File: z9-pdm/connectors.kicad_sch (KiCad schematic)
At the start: 11 parts, among them J10 RedCubeTerminal, J11 RedCubeTerminal, J12 Wago 12 pin 1 level 3.5mm 260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, J16 JST GH, J17 Wago 12 pin 1 level 3.5mm 260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, J19 Wago 12 pin 1 level 3.5mm 260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, J200 TE_DT15-12PC-B016 -Conn_01x12, J201 TE_DT15-12PC-B016 -Conn_01x12, J202 TE_DT15-12PC-B016 -Conn_01x12, J203 TE_DT15-12PC-B016 -Conn_01x12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

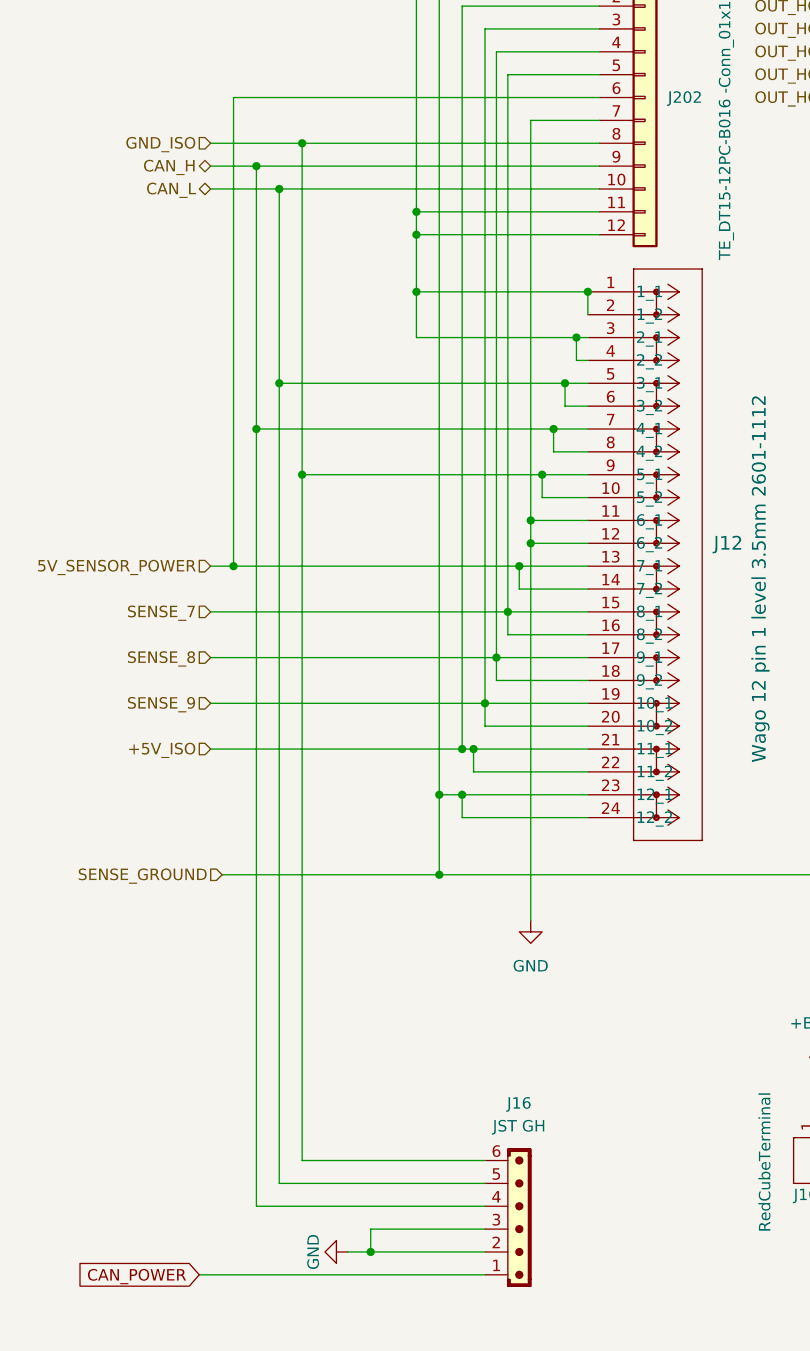
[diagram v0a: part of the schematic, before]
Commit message: laypout ad section canl/h swap
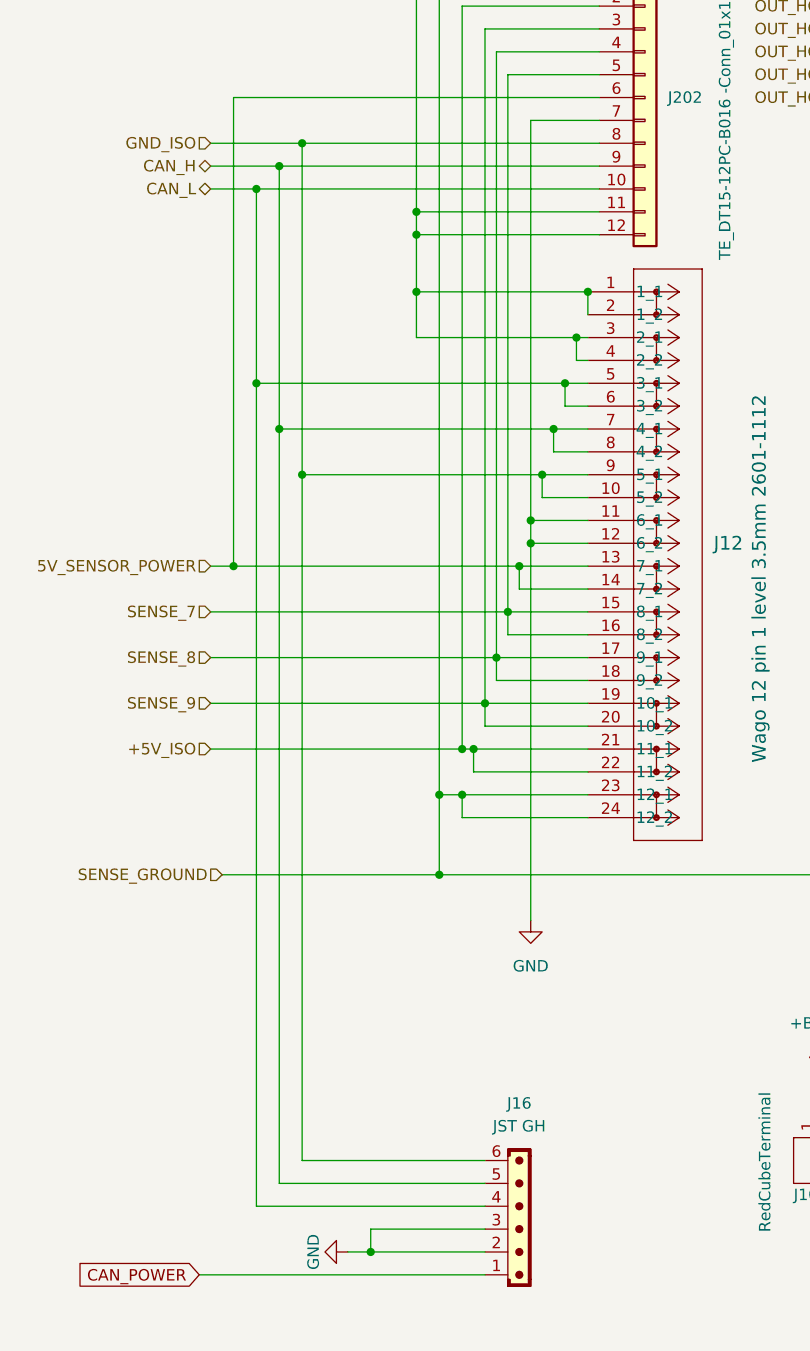
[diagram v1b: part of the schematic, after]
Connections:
- net CAN_H: now also J16.5; no longer J16.4
- net CAN_L: now also J16.4; no longer J16.5

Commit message: routing
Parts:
- J11: Voltage (none) -> GROUND
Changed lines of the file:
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@@
 			)
 		)
-		(property "Voltage" ""
+		(property "Voltage" "GROUND"
 			(at 107.95 162.56 90)
 			(effects

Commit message: new fuse and ideal diode
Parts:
- J10, J11, J12, J17, J19, J200, J201, J202, J203, J21: now not fitted; now left out of the parts list
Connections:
- net +12V_VIPOWER is gone; now on net +BATT: J12.1 (1_1), J12.2 (1_2), J12.3 (2_1), J12.4 (2_2), J202.11 (Pin_11), J202.12 (Pin_12)
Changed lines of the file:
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@@
 		(unit 1)
 		(exclude_from_sim no)
-		(in_bom yes)
+		(in_bom no)
 		(on_board yes)
-		(dnp no)
+		(dnp yes)
 		(property "Reference" "J17"
 			(at 270.51 92.7099 0)
@@
 		(unit 1)
 		(exclude_from_sim no)
-		(in_bom yes)
-		(on_board yes)
-		(dnp no)
+		(in_bom no)
+		(on_board no)
+		(dnp yes)
 		(property "Reference" "J11"
 			(at 110.49 157.48 90)
@@
 		(unit 1)
 		(exclude_from_sim no)
-		(in_bom yes)
+		(in_bom no)
 		(on_board yes)
-		(dnp no)
+		(dnp yes)
 		(property "Reference" "J202"
 			(at 83.82 43.1799 0)
@@
 			)
 		)
-		(property "Value" "+12V_VIPOWER"
+		(property "Value" "+BATT"
 			(at 25.4 21.59 0)
 			(effects
@@
 		(unit 1)
 		(exclude_from_sim no)
-		(in_bom yes)
+		(in_bom no)
 		(on_board yes)
-		(dnp no)
+		(dnp yes)
 		(property "Reference" "J21"
 			(at 143.51 92.7099 0)
@@
 		(unit 1)
 		(exclude_from_sim no)
-		(in_bom yes)
+		(in_bom no)
 		(on_board yes)
-		(dnp no)
+		(dnp yes)
 		(property "Reference" "J200"
 			(at 138.43 43.1799 0)
@@
 		(unit 1)
 		(exclude_from_sim no)
-		(in_bom yes)
+		(in_bom no)
 		(on_board yes)
-		(dnp no)
+		(dnp yes)
 		(property "Reference" "J201"
 			(at 198.12 43.1799 0)
@@
 		(unit 1)
 		(exclude_from_sim no)
-		(in_bom yes)
+		(in_bom no)
 		(on_board yes)
-		(dnp no)
+		(dnp yes)
 		(property "Reference" "J203"
 			(at 265.43 43.1799 0)
@@
 		(unit 1)
 		(exclude_from_sim no)
-		(in_bom yes)
+		(in_bom no)
 		(on_board yes)
-		(dnp no)
+		(dnp yes)
 		(property "Reference" "J10"
 			(at 97.79 165.1 90)
@@
 		(unit 1)
 		(exclude_from_sim no)
-		(in_bom yes)
+		(in_bom no)
 		(on_board yes)
-		(dnp no)
+		(dnp yes)
 		(property "Reference" "J19"
 			(at 220.98 92.7099 0)
@@
 		(unit 1)
 		(exclude_from_sim no)
-		(in_bom yes)
+		(in_bom no)
 		(on_board yes)
-		(dnp no)
+		(dnp yes)
 		(property "Reference" "J12"
 			(at 88.9 92.7099 0)

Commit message: post 5v lay references lost
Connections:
- net +5V_ISO is gone; now on net GND: J12.21 (11_1), J12.22 (11_2), J202.2 (Pin_2)
- net CAN_POWER: now also J12.10 (5_2), J12.9 (5_1), J202.7 (Pin_7)
- net GND: no longer J12.11 (6_1), J12.12 (6_2), J202.7 (Pin_7)
- net GND_ISO: now also J12.11 (6_1), J12.12 (6_2); no longer J12.10 (5_2), J12.9 (5_1)
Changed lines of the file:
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@@
 	)
 	(junction
-		(at 68.58 90.17)
-		(diameter 0)
-		(color 0 0 0 0)
-	)
-	(junction
 		(at 55.88 105.41)
 		(diameter 0)
@@
 	)
 	(junction
-		(at 40.64 30.48)
+		(at 72.39 45.72)
 		(diameter 0)
 		(color 0 0 0 0)
 	)
 	(junction
-		(at 43.18 85.09)
+		(at 40.64 30.48)
 		(diameter 0)
 		(color 0 0 0 0)
@@
 	)
 	(junction
+		(at 74.93 85.09)
+		(diameter 0)
+		(color 0 0 0 0)
+	)
+	(junction
 		(at 165.1 50.8)
 		(diameter 0)
@@
 	)
 	(junction
-		(at 256.54 74.93)
+		(at 68.58 48.26)
 		(diameter 0)
 		(color 0 0 0 0)
 	)
 	(junction
-		(at 129.54 64.77)
+		(at 256.54 74.93)
 		(diameter 0)
 		(color 0 0 0 0)
 	)
 	(junction
-		(at 129.54 105.41)
+		(at 129.54 64.77)
 		(diameter 0)
 		(color 0 0 0 0)
 	)
 	(junction
-		(at 232.41 100.33)
+		(at 129.54 105.41)
 		(diameter 0)
 		(color 0 0 0 0)
 	)
 	(junction
-		(at 74.93 85.09)
+		(at 232.41 100.33)
 		(diameter 0)
 		(color 0 0 0 0)
@@
 	(wire
 		(pts
+			(xy 72.39 45.72) (xy 76.2 45.72)
+		)
+		(stroke
+			(width 0)
+			(type default)
+		)
+	)
+	(wire
+		(pts
 			(xy 165.1 110.49) (xy 189.23 110.49)
 		)
@@
 	(wire
 		(pts
-			(xy 43.18 48.26) (xy 43.18 85.09)
+			(xy 43.18 48.26) (xy 43.18 161.29)
 		)
 		(stroke
@@
 	(wire
 		(pts
-			(xy 68.58 45.72) (xy 68.58 90.17)
-		)
-		(stroke
-			(width 0)
-			(type default)
-		)
-	)
-	(wire
-		(pts
 			(xy 48.26 120.65) (xy 74.93 120.65)
 		)
@@
 	(wire
 		(pts
+			(xy 50.8 115.57) (xy 50.8 135.89)
+		)
+		(stroke
+			(width 0)
+			(type default)
+		)
+	)
+	(wire
+		(pts
 			(xy 50.8 168.91) (xy 50.8 171.45)
 		)
@@
 	(wire
 		(pts
-			(xy 104.14 48.26) (xy 104.14 50.8)
+			(xy 68.58 48.26) (xy 76.2 48.26)
 		)
 		(stroke
@@
 	(wire
 		(pts
-			(xy 68.58 90.17) (xy 68.58 121.92)
+			(xy 104.14 48.26) (xy 104.14 50.8)
 		)
 		(stroke
@@
 	(wire
 		(pts
-			(xy 76.2 45.72) (xy 68.58 45.72)
-		)
-		(stroke
-			(width 0)
-			(type default)
-		)
-	)
-	(wire
-		(pts
 			(xy 104.14 90.17) (xy 129.54 90.17)
 		)
@@
 	(wire
 		(pts
-			(xy 232.41 110.49) (xy 232.41 120.65)
+			(xy 68.58 48.26) (xy 68.58 90.17)
 		)
 		(stroke
@@
 	(wire
 		(pts
-			(xy 43.18 85.09) (xy 74.93 85.09)
+			(xy 232.41 110.49) (xy 232.41 120.65)
 		)
 		(stroke
@@
 	(wire
 		(pts
-			(xy 33.02 115.57) (xy 50.8 115.57)
-		)
-		(stroke
-			(width 0)
-			(type default)
-		)
-	)
-	(wire
-		(pts
 			(xy 116.84 115.57) (xy 129.54 115.57)
 		)
@@
 	(wire
 		(pts
+			(xy 72.39 85.09) (xy 74.93 85.09)
+		)
+		(stroke
+			(width 0)
+			(type default)
+		)
+	)
+	(wire
+		(pts
 			(xy 189.23 92.71) (xy 189.23 90.17)
 		)
@@
 	(wire
 		(pts
-			(xy 43.18 85.09) (xy 43.18 161.29)
-		)
-		(stroke
-			(width 0)
-			(type default)
-		)
-	)
-	(wire
-		(pts
 			(xy 43.18 161.29) (xy 63.5 161.29)
 		)
@@
 	(wire
 		(pts
+			(xy 33.02 45.72) (xy 72.39 45.72)
+		)
+		(stroke
+			(width 0)
+			(type default)
+		)
+	)
+	(wire
+		(pts
 			(xy 184.15 35.56) (xy 184.15 85.09)
 		)
@@
 	(wire
 		(pts
+			(xy 72.39 45.72) (xy 72.39 85.09)
+		)
+		(stroke
+			(width 0)
+			(type default)
+		)
+	)
+	(wire
+		(pts
 			(xy 232.41 53.34) (xy 232.41 55.88)
 		)
@@
 	(wire
 		(pts
-			(xy 43.18 48.26) (xy 76.2 48.26)
+			(xy 43.18 48.26) (xy 68.58 48.26)
 		)
 		(stroke
@@
 		)
 	)
+	(global_label "CAN_POWER"
+		(shape input)
+		(at 33.02 45.72 180)
+		(fields_autoplaced yes)
+		(effects
+			(font
+				(size 1.27 1.27)
+			)
+			(justify right)
+		)
+		(property "Intersheetrefs" "${INTERSHEET_REFS}"
+			(at 18.9072 45.72 0)
+			(effects
+				(font
+					(size 1.27 1.27)
+				)
+				(justify right)
+			)
+		)
+	)
 	(hierarchical_label "GND_ISO"
 		(shape input)
@@
 		)
 	)
-	(hierarchical_label "+5V_ISO"
-		(shape input)
-		(at 33.02 115.57 180)
-		(effects
-			(font
-				(size 1.27 1.27)
-			)
-			(justify right)
-		)
-	)
 	(hierarchical_label "SENSE_2"
 		(shape input)
@@
 		(exclude_from_sim no)
 		(in_bom no)
-		(on_board no)
+		(on_board yes)
 		(dnp yes)
 		(property "Reference" "J11"
@@
 	(symbol
 		(lib_id "power:GND")
-		(at 68.58 121.92 0)
+		(at 50.8 135.89 0)
 		(unit 1)
 		(exclude_from_sim no)
@@
 		(fields_autoplaced yes)
 		(property "Reference" "#PWR0708"
-			(at 68.58 128.27 0)
+			(at 50.8 142.24 0)
 			(effects
 				(font
@@
 		)
 		(property "Value" "GND"
-			(at 68.58 127 0)
+			(at 50.8 140.97 0)
 			(effects
 				(font
@@
 		)
 		(property "Footprint" ""
-			(at 68.58 121.92 0)
+			(at 50.8 135.89 0)
 			(effects
 				(font
@@
 		)
 		(property "Datasheet" ""
-			(at 68.58 121.92 0)
+			(at 50.8 135.89 0)
 			(effects
 				(font
@@
 		)
 		(property "Description" "Power symbol creates a global label with name \"GND\" , ground"
-			(at 68.58 121.92 0)
+			(at 50.8 135.89 0)
 			(effects
 				(font

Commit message: pre final pdm erc
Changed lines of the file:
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@@
 	)
 	(junction
-		(at 40.64 30.48)
-		(diameter 0)
-		(color 0 0 0 0)
-	)
-	(junction
 		(at 232.41 120.65)
 		(diameter 0)
@@
 	(wire
 		(pts
-			(xy 40.64 24.13) (xy 40.64 30.48)
-		)
-		(stroke
-			(width 0)
-			(type default)
-		)
-	)
-	(wire
-		(pts
 			(xy 189.23 77.47) (xy 189.23 74.93)
 		)
@@
 	(wire
 		(pts
-			(xy 25.4 30.48) (xy 40.64 30.48)
-		)
-		(stroke
-			(width 0)
-			(type default)
-		)
-	)
-	(wire
-		(pts
 			(xy 100.33 151.13) (xy 100.33 156.21)
 		)
@@
 	(wire
 		(pts
-			(xy 40.64 30.48) (xy 45.72 30.48)
+			(xy 25.4 30.48) (xy 45.72 30.48)
 		)
 		(stroke
@@
 					(unit 1)
 				)
-			)
-		)
-	)
-	(symbol
-		(lib_id "power:PWR_FLAG")
-		(at 40.64 24.13 0)
-		(unit 1)
-		(exclude_from_sim no)
-		(in_bom yes)
-		(on_board yes)
-		(dnp no)
-		(property "Reference" "#FLG01"
-			(at 40.64 22.225 0)
-			(effects
-				(font
-					(size 1.27 1.27)
-				)
-				(hide yes)
-			)
-		)
-		(property "Value" "PWR_FLAG"
-			(at 40.64 20.32 0)
-			(effects
-				(font
-					(size 1.27 1.27)
-				)
-			)
-		)
-		(property "Footprint" ""
-			(at 40.64 24.13 0)
-			(effects
-				(font
-					(size 1.27 1.27)
-				)
-				(hide yes)
-			)
-		)
-		(property "Datasheet" "~"
-			(at 40.64 24.13 0)
-			(effects
-				(font
-					(size 1.27 1.27)
-				)
-				(hide yes)
-			)
-		)
-		(property "Description" "Special symbol for telling ERC where power comes from"
-			(at 40.64 24.13 0)
-			(effects
-				(font
-					(size 1.27 1.27)
-				)
-				(hide yes)
-			)
-		)
-		(pin "1"
-		)
-		(instances
-			(project ""
-				(path "/b643db5c-578e-4b48-aafc-cc4190db582a/651fe70f-48a4-454d-84e2-56b28624b7c9"
-					(reference "#FLG01")
-					(unit 1)
-				)

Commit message: x
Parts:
- J10: renamed from J21; now in the parts list
- J11: renamed from J200; now in the parts list
- J12: renamed from J19; now in the parts list
- J13: renamed from J201; now in the parts list
- J14: renamed from J17; now in the parts list
- J15: renamed from J203; now in the parts list
- J5: renamed from J16; FT Rotation Offset (none) -> 180
- J6: renamed from J12; now in the parts list
- J7: renamed from J202; now in the parts list
- J8: renamed from J10; now in the parts list
- J9: renamed from J11; Voltage GROUND -> (none); now in the parts list

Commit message: passes sch drc
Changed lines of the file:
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@@
 		)
 		(property "Value" "+BATT"
-			(at 27.94 25.3999 0)
-			(effects
-				(font
-					(size 1.27 1.27)
-				)
-				(justify left)
+			(at 25.4 21.59 0)
+			(effects
+				(font
+					(size 1.27 1.27)
+				)
 			)
 		)
@@
 		)
 		(property "Value" "GND"
-			(at 167.64 123.1899 0)
-			(effects
-				(font
-					(size 1.27 1.27)
-				)
-				(justify left)
+			(at 165.1 127 0)
+			(effects
+				(font
+					(size 1.27 1.27)
+				)
 			)
 		)
@@
 		)
 		(property "Value" "GND"
-			(at 53.34 137.1599 0)
-			(effects
-				(font
-					(size 1.27 1.27)
-				)
-				(justify left)
+			(at 50.8 140.97 0)
+			(effects
+				(font
+					(size 1.27 1.27)
+				)
 			)
 		)
@@
 		)
 		(property "Value" "GND"
-			(at 106.68 123.1899 0)
-			(effects
-				(font
-					(size 1.27 1.27)
-				)
-				(justify left)
+			(at 104.14 127 0)
+			(effects
+				(font
+					(size 1.27 1.27)
+				)
 			)
 		)
@@
 		)
 		(property "Value" "+BATT"
-			(at 102.87 149.8599 0)
-			(effects
-				(font
-					(size 1.27 1.27)
-				)
-				(justify left)
-			)
-		)
+			(at 100.33 146.05 0)
+			(effects
+				(font
+					(size 1.27 1.27)
+				)
+			)
+		)
